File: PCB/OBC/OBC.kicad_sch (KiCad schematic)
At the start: 1 part, among them J1 Conn_02x24_Odd_Even

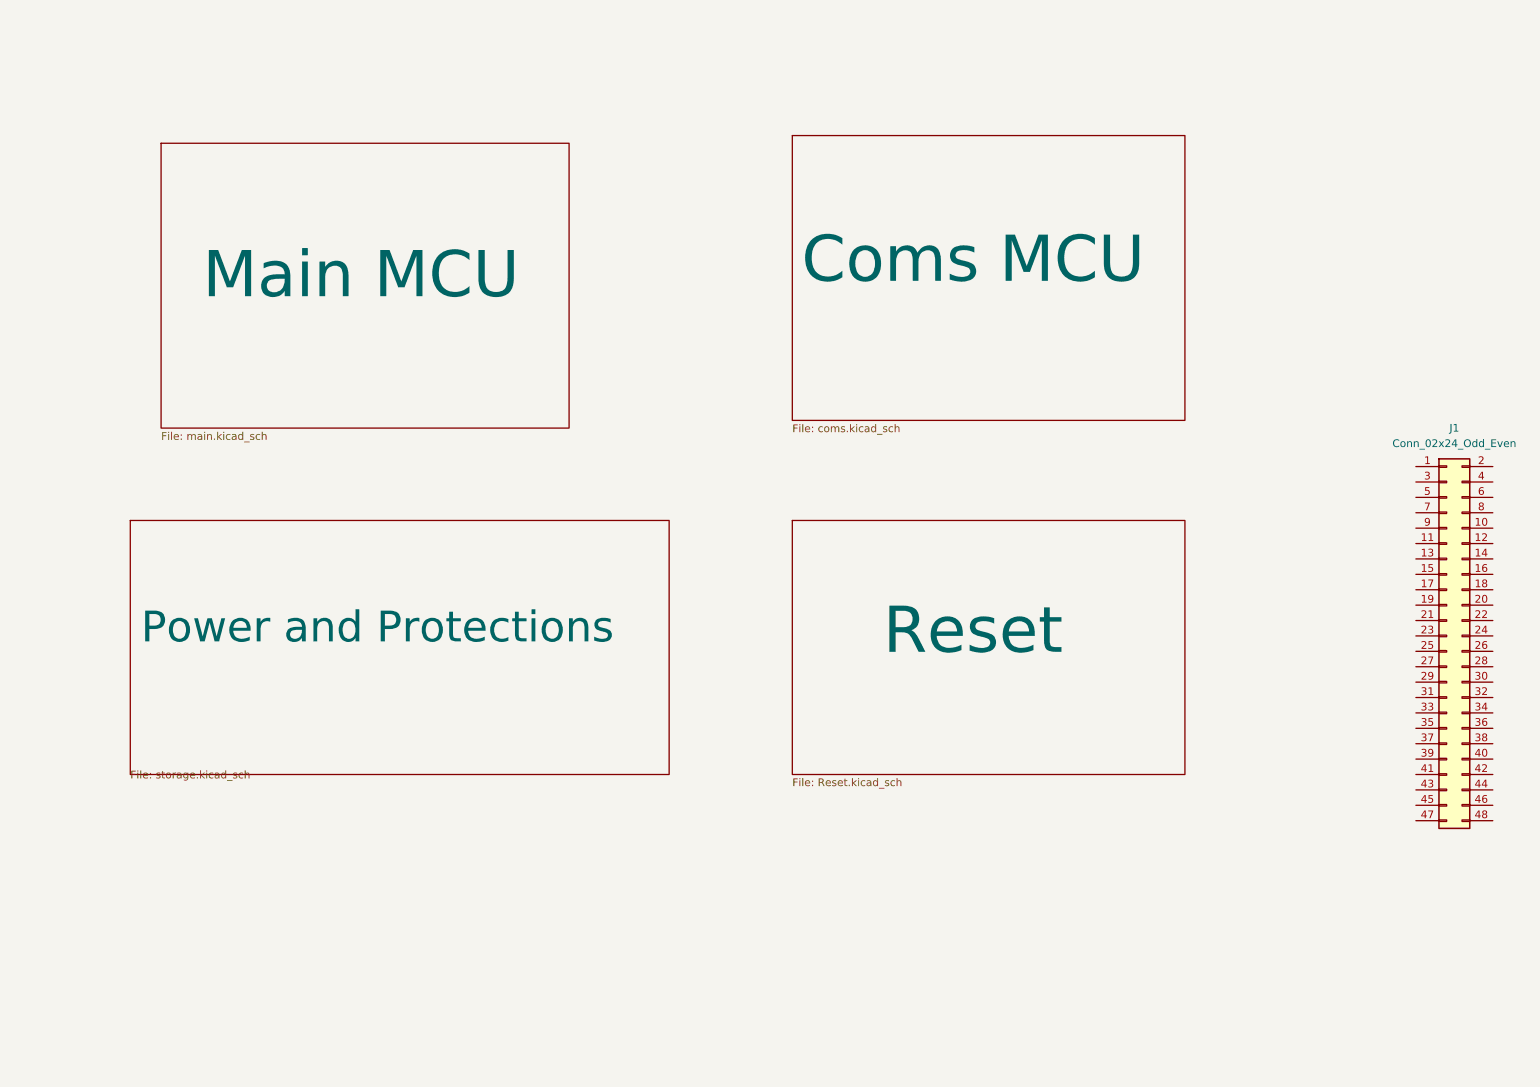
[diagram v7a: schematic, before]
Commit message: Add: Can bus
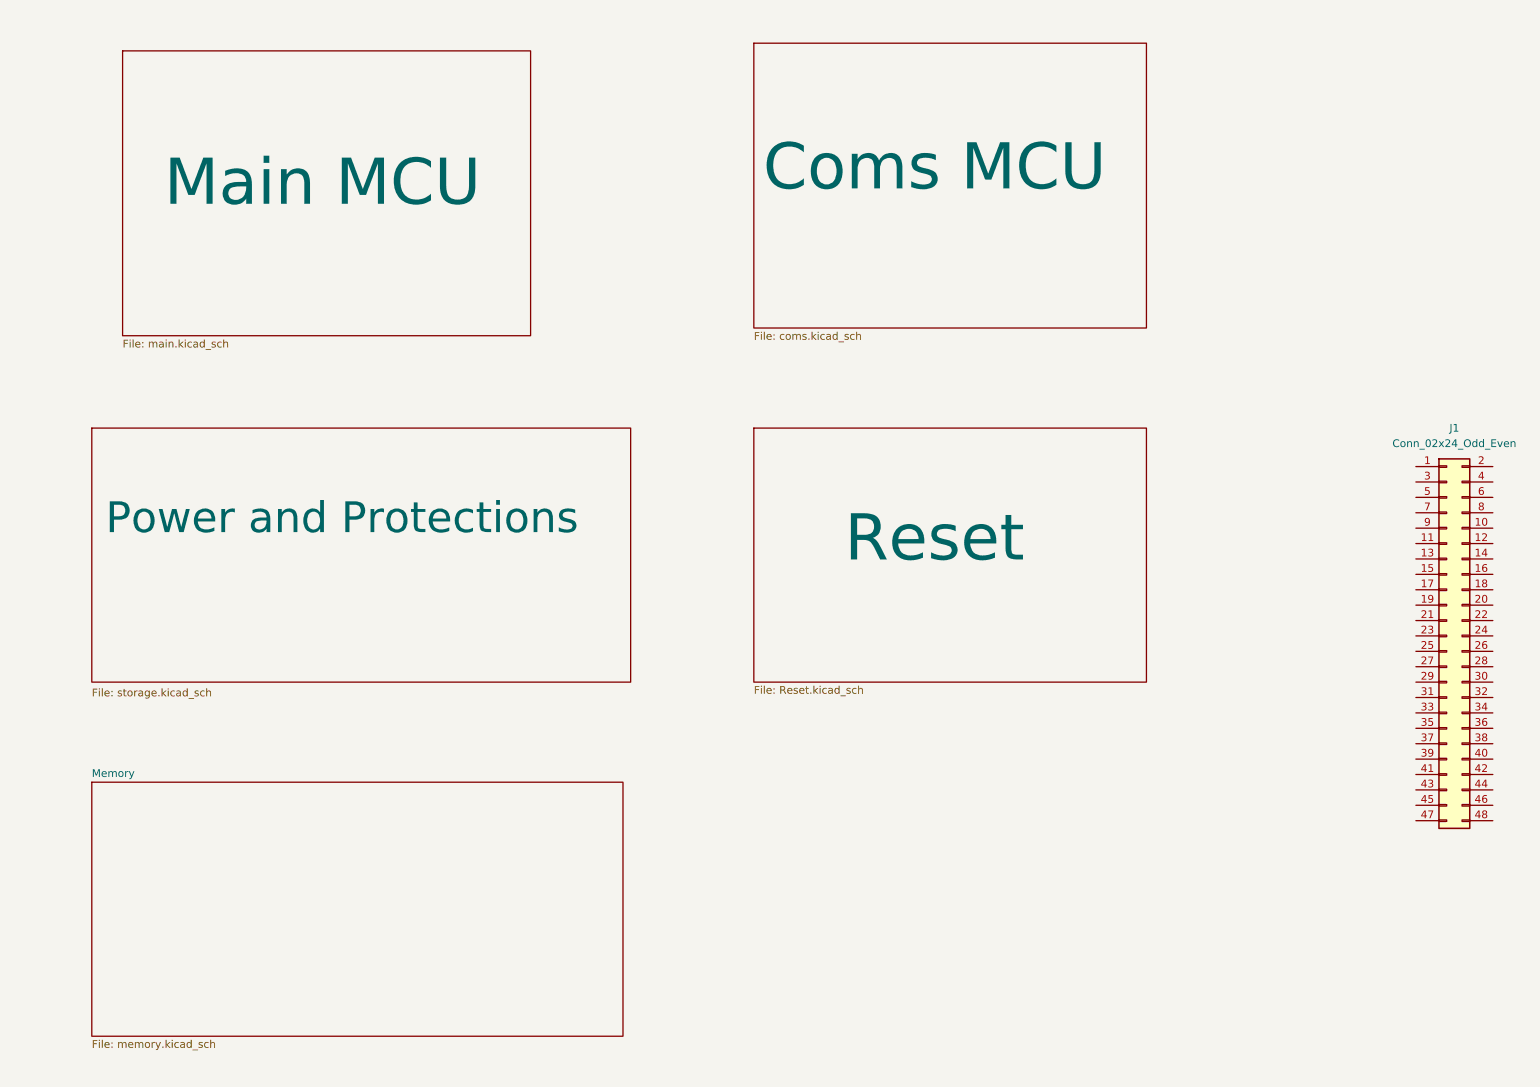
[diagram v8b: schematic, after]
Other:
- added sheet Memory (memory.kicad_sch)
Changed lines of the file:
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@@
 	)
 	(sheet
-		(at 40.64 36.83)
+		(at 34.29 21.59)
 		(size 67.31 46.99)
 		(exclude_from_sim no)
@@
 		)
 		(property "Sheetname" "Main MCU"
-			(at 47.498 62.992 0)
+			(at 41.148 47.752 0)
 			(effects
 				(font
@@
 		)
 		(property "Sheetfile" "main.kicad_sch"
-			(at 40.64 84.43 0)
+			(at 34.29 69.19 0)
 			(effects
 				(font
@@
 	)
 	(sheet
-		(at 144.78 35.56)
+		(at 138.43 20.32)
 		(size 64.77 46.99)
 		(exclude_from_sim no)
@@
 		)
 		(property "Sheetname" "Coms MCU"
-			(at 146.304 60.452 0)
+			(at 139.954 45.212 0)
 			(effects
 				(font
@@
 		)
 		(property "Sheetfile" "coms.kicad_sch"
-			(at 144.78 83.16 0)
+			(at 138.43 67.92 0)
 			(effects
 				(font
@@
 	)
 	(sheet
-		(at 144.78 99.06)
+		(at 138.43 83.82)
 		(size 64.77 41.91)
 		(exclude_from_sim no)
@@
 		)
 		(property "Sheetname" "Reset"
-			(at 159.766 121.666 0)
+			(at 153.416 106.426 0)
 			(effects
 				(font
@@
 		)
 		(property "Sheetfile" "Reset.kicad_sch"
-			(at 144.78 141.5546 0)
+			(at 138.43 126.3146 0)
 			(effects
 				(font
@@
 	)
 	(sheet
-		(at 35.56 99.06)
+		(at 29.21 83.82)
 		(size 88.9 41.91)
 		(exclude_from_sim no)
@@
 		)
 		(property "Sheetname" "Power and Protections"
-			(at 37.338 119.634 0)
+			(at 31.496 101.6 0)
 			(effects
 				(font
@@
 		)
 		(property "Sheetfile" "storage.kicad_sch"
-			(at 35.56 140.2846 0)
+			(at 29.21 126.746 0)
 			(effects
 				(font
@@
 				)
 			)
+		)
+	)
+	(sheet
+		(at 29.21 142.24)
+		(size 87.63 41.91)
+		(exclude_from_sim no)
+		(in_bom yes)
+		(on_board yes)
+		(dnp no)
+		(fields_autoplaced yes)
+		(stroke
+			(width 0.1524)
+			(type solid)
+		)
+		(fill
+			(color 0 0 0 0.0000)
+		)
+		(property "Sheetname" "Memory"
+			(at 29.21 141.5284 0)
+			(effects
+				(font
+					(size 1.27 1.27)
+				)
+				(justify left bottom)
+			)
+		)
+		(property "Sheetfile" "memory.kicad_sch"
+			(at 29.21 184.7346 0)
+			(effects
+				(font
+					(size 1.27 1.27)
+				)
+				(justify left top)
+			)
+		)
+		(instances
+			(project "OBC"
+				(path "/e2c03eef-3b12-44a7-ba52-633d5337a24a"
+					(page "6")
+				)
+			)
